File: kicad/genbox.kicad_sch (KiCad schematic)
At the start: 19 parts, among them SW15 SW_SPST, SW16 SW_SPST, SW17 SW_SPST, SW18 SW_SPST

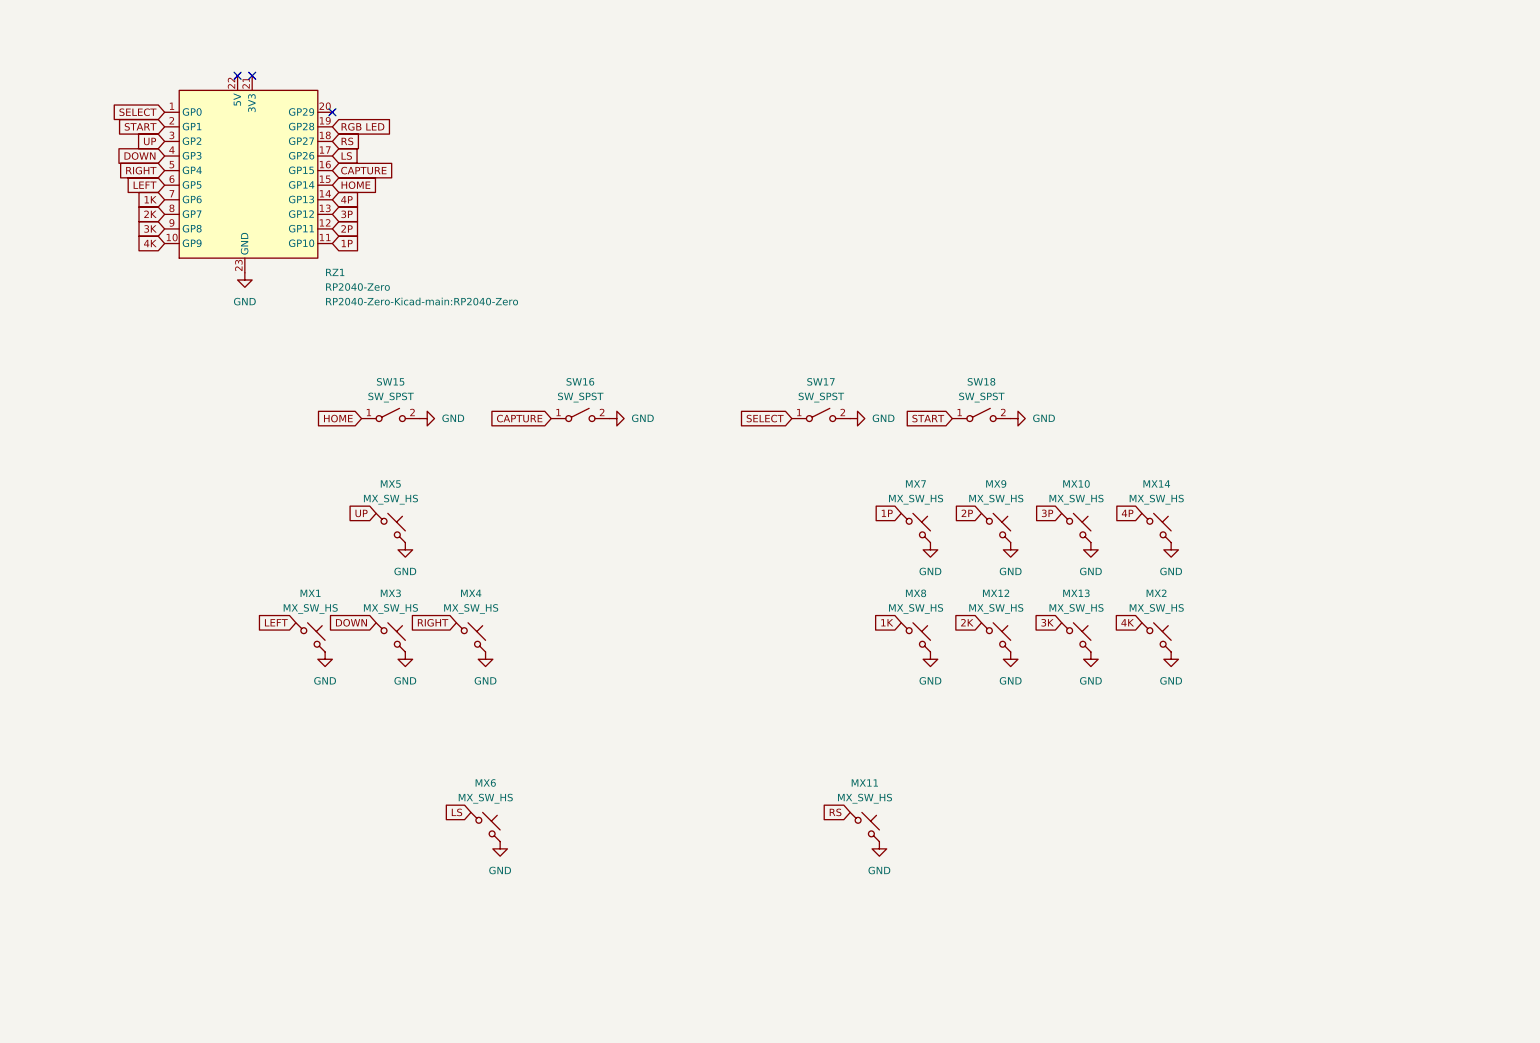
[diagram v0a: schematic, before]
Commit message: fixed gitignore
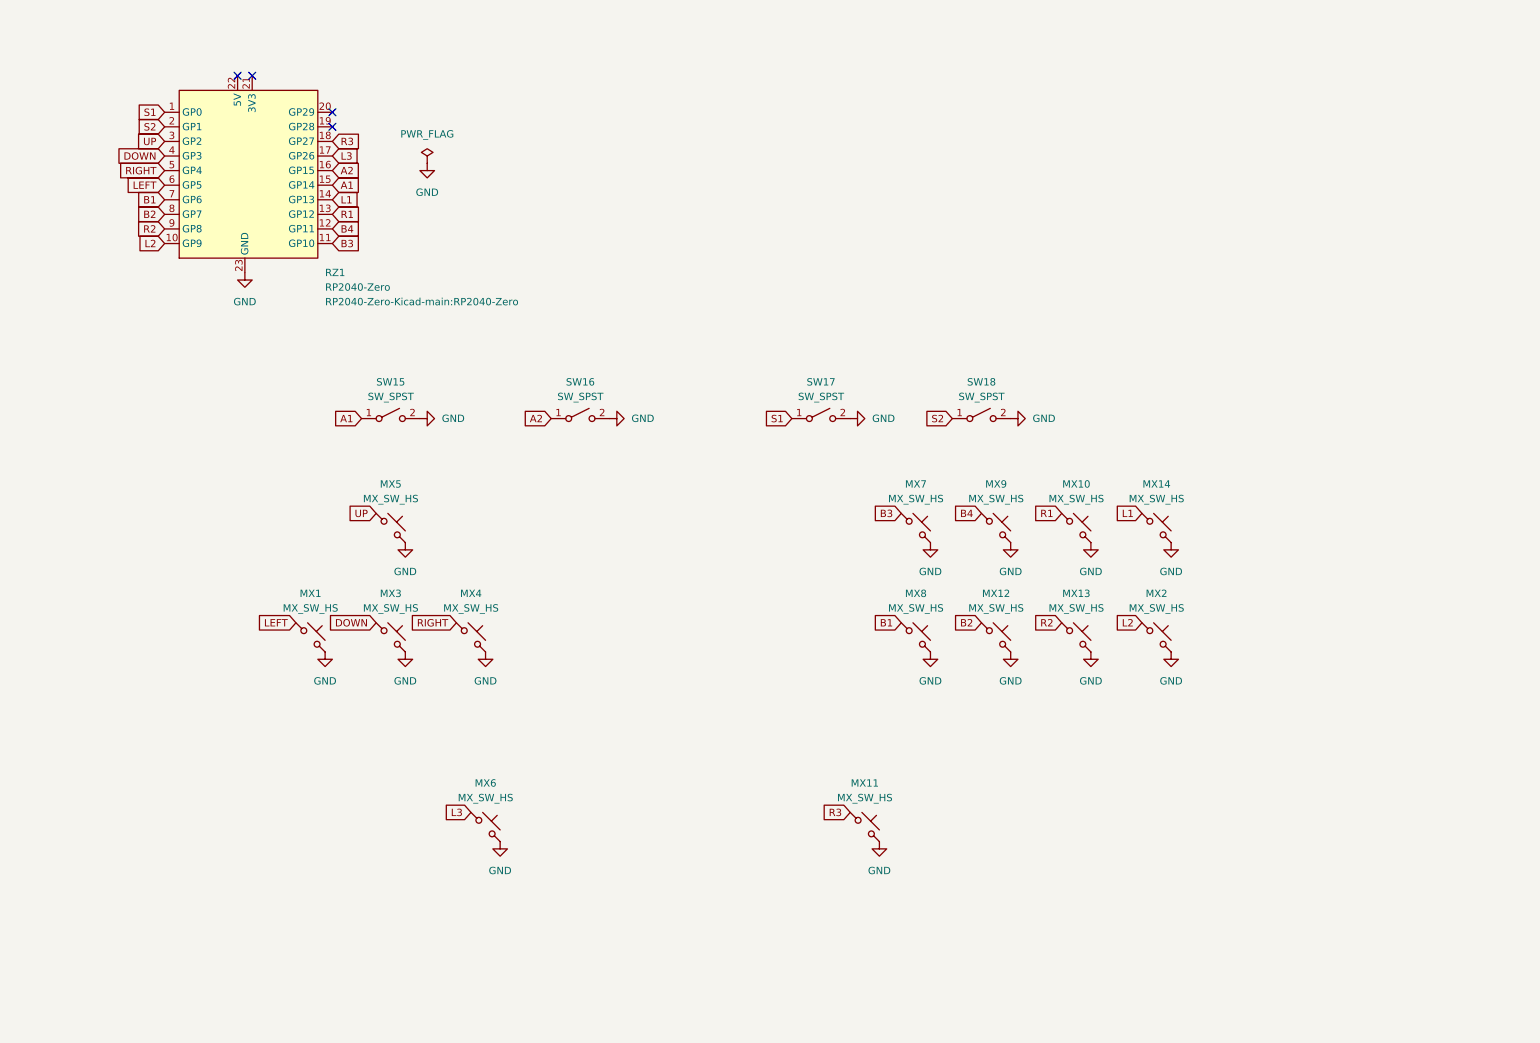
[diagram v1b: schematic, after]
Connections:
- net 1K renamed B1
- net 1P renamed B3
- net 2K renamed B2
- net 2P renamed B4
- net 3K renamed R2
- net 3P renamed R1
- net 4K renamed L2
- net 4P renamed L1
- net CAPTURE renamed A2
- net HOME renamed A1
- net LS renamed L3
- net RGB LED: no longer names the net of RZ1.19 (GP28)
- net RS renamed R3
- net SELECT renamed S1
- net START renamed S2
- no-connect marks 3 -> 4

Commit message: rework p1
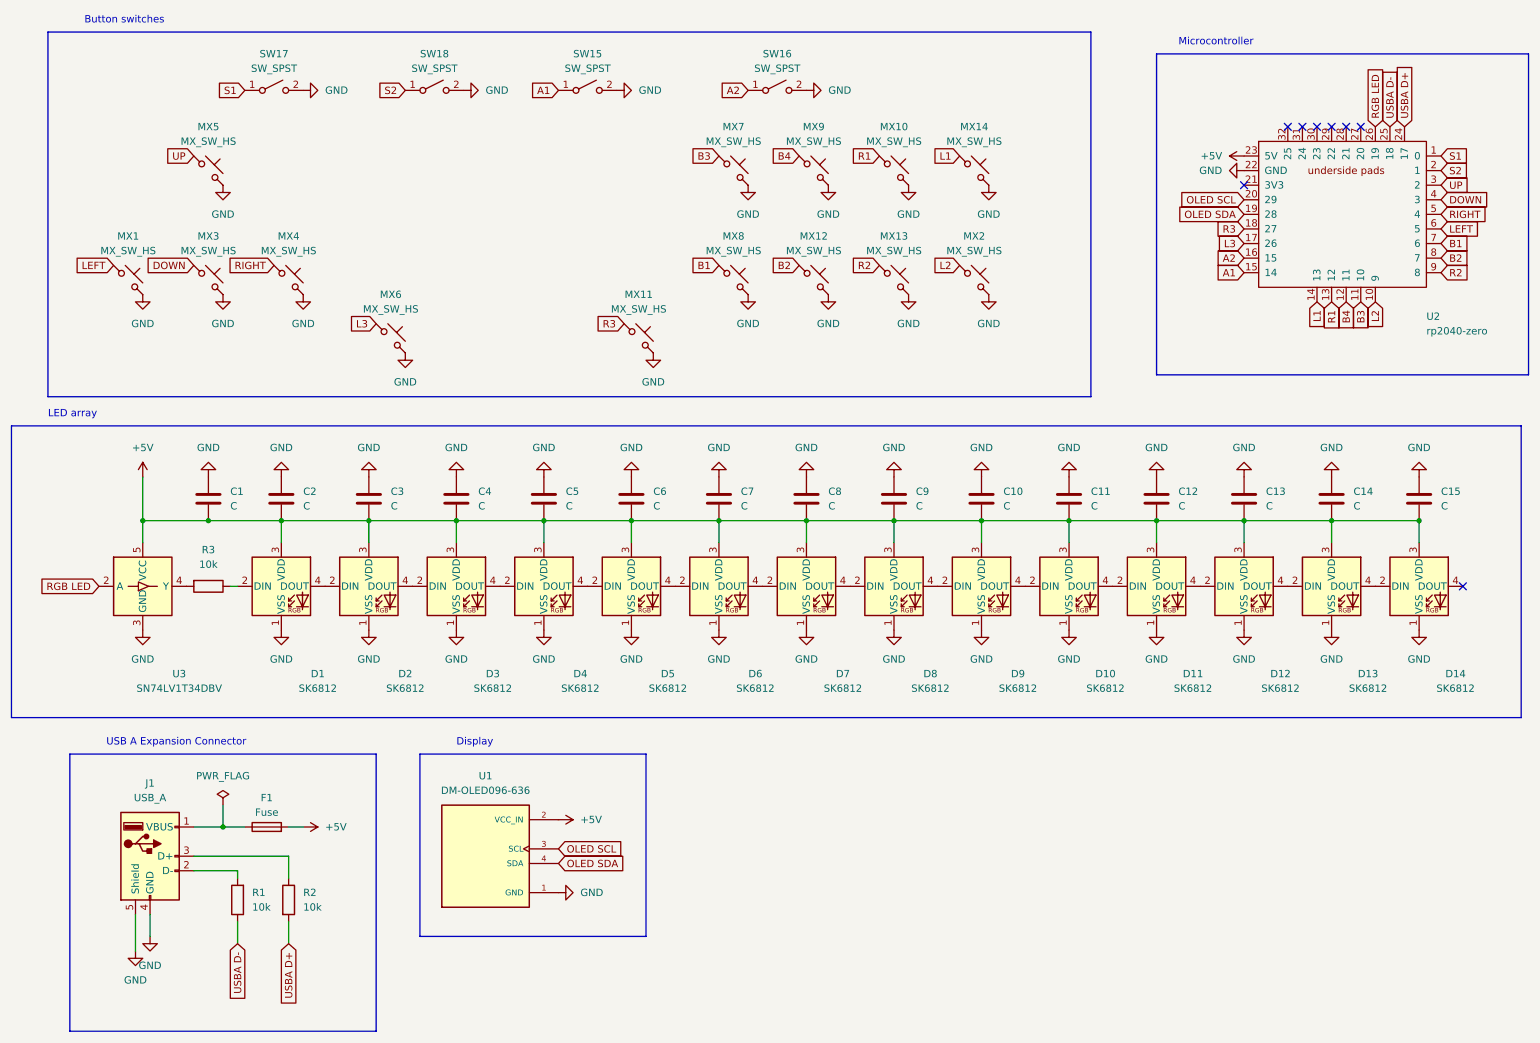
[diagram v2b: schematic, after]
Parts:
- removed RZ1: RP2040-Zero, RP2040-Zero-Kicad-main:RP2040-Zero, symbol rp2040-zero:RP2040-Zero
- added C1, C10, C11, C12, C13, C14, C15, C2, C3, C4, C5, C6, C7, C8, C9: C, Capacitor_SMD:C_0805_2012Metric_Pad1.18x1.45mm_HandSolder, symbol Device:C
- added D1, D10, D11, D12, D13, D14, D2, D3, D4, D5, D6, D7, D8, D9: SK6812, haku:SK6812-MINI-E_MX, symbol LED:SK6812
- added F1: Fuse, Fuse:Fuse_0805_2012Metric_Pad1.15x1.40mm_HandSolder, symbol Device:Fuse
- added J1: USB_A, Connector_USB:USB_A_Receptacle_GCT_USB1046, symbol Connector:USB_A
- added R1, R2, R3: 10k, Resistor_SMD:R_0603_1608Metric_Pad0.98x0.95mm_HandSolder, symbol Device:R
- added U1: DM-OLED096-636, DM-OLED096-636:MODULE_DM-OLED096-636, symbol OLED096:DM-OLED096-636
- added U2: rp2040-zero, mcu:rp2040-zero-smd-pads, symbol mcu:rp2040-zero-pads
- added U3: SN74LV1T34DBV, Package_TO_SOT_SMD:SOT-23-5, symbol Logic_LevelTranslator:SN74LV1T34DBV
- MX1, MX10, MX11, MX12, MX13, MX14, MX2, MX3, MX4, MX5, MX6, MX7, MX8, MX9: LCSC Part # (none) -> C5184526
- SW15, SW16, SW17, SW18: footprint Button_Switch_THT:SW_PUSH_6mm_H7.3mm -> haku:SW_PUSH-12mm_centered; LCSC Part # (none) -> C455212
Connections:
- net A1: now also U2.15 (14)
- net A2: now also U2.16 (15)
- net B1: now also U2.7 (6)
- net B2: now also U2.8 (7)
- net B3: now also U2.11 (10)
- net B4: now also U2.12 (11)
- net DOWN: now also U2.4 (3)
- net GND: now also C1.1, C10.1, C11.1, C12.1, C13.1, C14.1, C15.1, C2.1, C3.1, C4.1, C5.1, C6.1, C7.1, C8.1, C9.1, D1.1 (VSS), D10.1 (VSS), D11.1 (VSS), D12.1 (VSS), D13.1 (VSS), D14.1 (VSS), D2.1 (VSS), D3.1 (VSS), D4.1 (VSS), D5.1 (VSS), D6.1 (VSS), D7.1 (VSS), D8.1 (VSS), D9.1 (VSS), J1.4 (GND), J1.5 (Shield), U1.1 (GND), U2.22 (GND), U2.33 (GND), U3.3 (GND)
- net L1: now also U2.14 (13)
- net L2: now also U2.10 (9)
- net L3: now also U2.17 (26)
- net LEFT: now also U2.6 (5)
- net R1: now also U2.13 (12)
- net R2: now also U2.9 (8)
- net R3: now also U2.18 (27)
- net RIGHT: now also U2.5 (4)
- net S1: now also U2.1 (0)
- net S2: now also U2.2 (1)
- net UP: now also U2.3 (2)
- new net: D13.4 (DOUT), D14.2 (DIN)
- new net: D3.4 (DOUT), D4.2 (DIN)
- new net: D4.4 (DOUT), D5.2 (DIN)
- new net: D1.2 (DIN), R3.1
- new net: D1.4 (DOUT), D2.2 (DIN)
- new net: D6.4 (DOUT), D7.2 (DIN)
- new net: D7.4 (DOUT), D8.2 (DIN)
- new net: D8.4 (DOUT), D9.2 (DIN)
- new net: D10.2 (DIN), D9.4 (DOUT)
- new net: D5.4 (DOUT), D6.2 (DIN)
- new net: F1.1, J1.1 (VBUS)
- new net: J1.2 (D-), R1.2
- new net: J1.3 (D+), R2.1
- new net: D10.4 (DOUT), D11.2 (DIN)
- new net: R3.2, U3.4 (Y)
- new net: D11.4 (DOUT), D12.2 (DIN)
- new net: D2.4 (DOUT), D3.2 (DIN)
- new net: D12.4 (DOUT), D13.2 (DIN)
- new net +5V: C1.2, C10.2, C11.2, C12.2, C13.2, C14.2, C15.2, C2.2, C3.2, C4.2, C5.2, C6.2, C7.2, C8.2, C9.2, D1.3 (VDD), D10.3 (VDD), D11.3 (VDD), D12.3 (VDD), D13.3 (VDD), D14.3 (VDD), D2.3 (VDD), D3.3 (VDD), D4.3 (VDD), D5.3 (VDD), D6.3 (VDD), D7.3 (VDD), D8.3 (VDD), D9.3 (VDD), F1.2, U1.2 (VCC_IN), U2.23 (5V), U3.5 (VCC)
- new net OLED SCL: U1.3 (SCL), U2.20 (29)
- new net OLED SDA: U1.4 (SDA), U2.19 (28)
- new net RGB LED: U2.26 (19), U3.2 (A)
- new net USBA D+: R2.2, U2.24 (17)
- new net USBA D-: R1.1, U2.25 (18)
- no-connect marks 4 -> 8
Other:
- note added: "Button switches"
- note added: "Display"
- note added: "LED array"
- note added: "Microcontroller"
- note added: "USB A Expansion Connector"
- moved on the sheet: MX1, MX10, MX11, MX12, MX13, MX14, MX2, MX3, MX4, MX5, MX6, MX7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

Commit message: converted to freecad link branch
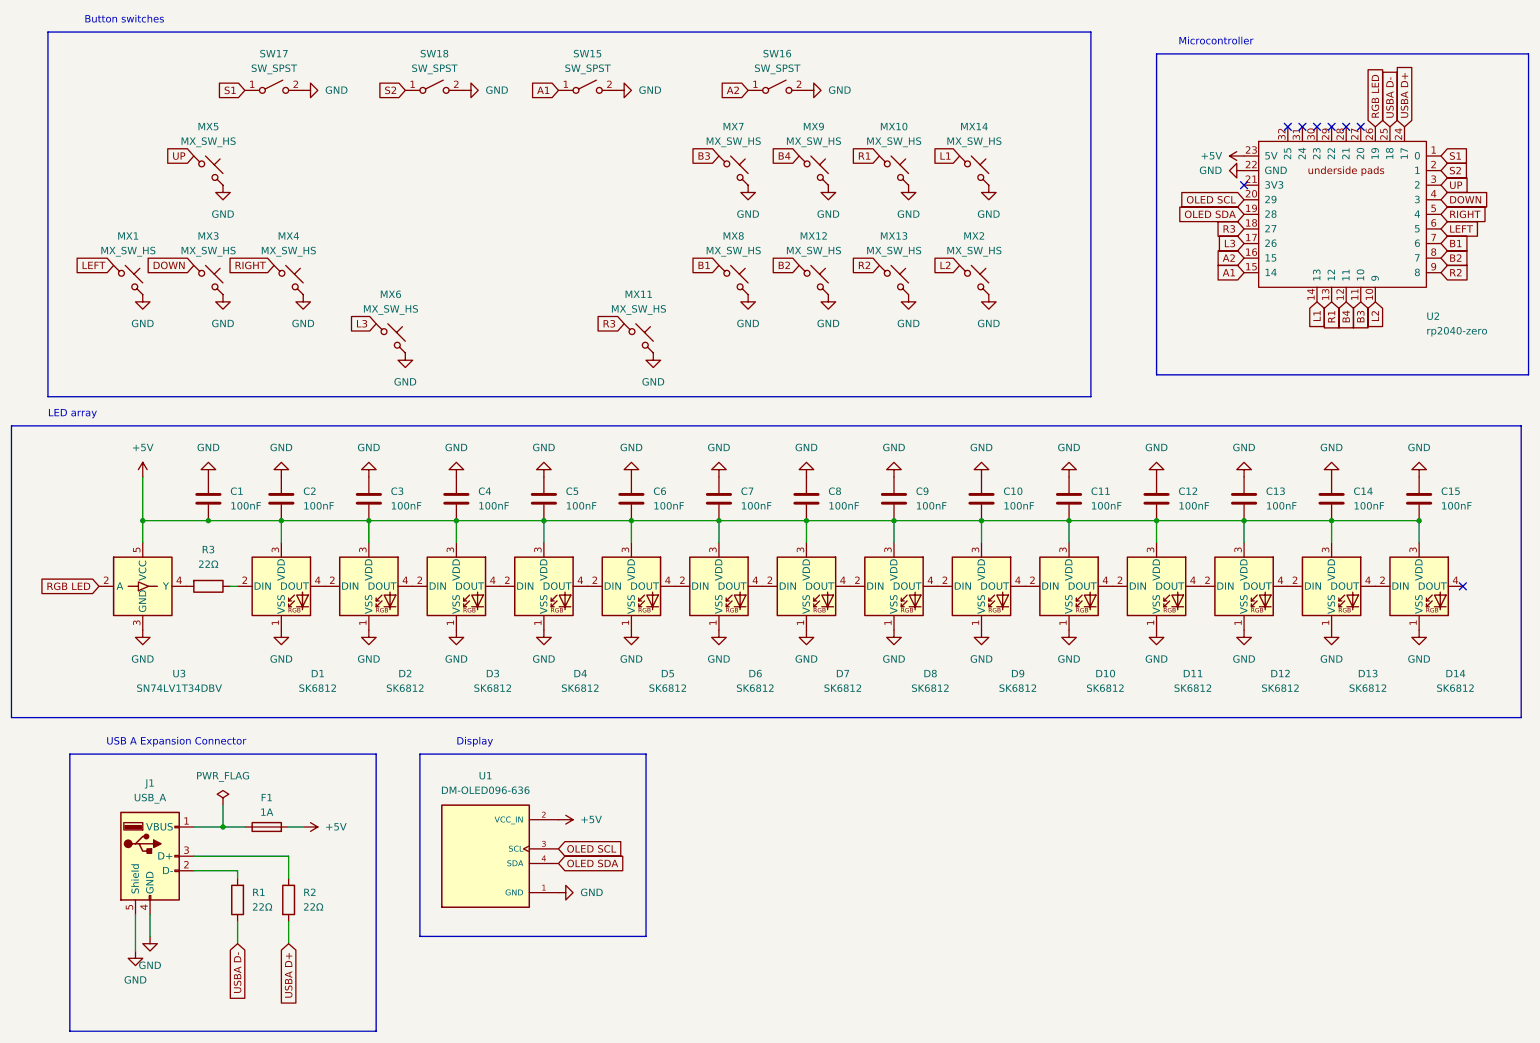
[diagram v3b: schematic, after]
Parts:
- C1, C10, C11, C12, C13, C14, C15, C2, C3, C4, C5, C6, C7, C8, C9: value C -> 100nF
- F1: value Fuse -> 1A
- R1, R2, R3: value 10k -> 22Ω
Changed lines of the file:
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@@
       (effects (font (size 1.27 1.27)) (justify left))
     )
-    (property "Value" "C" (at 187.96 101.6 0)
+    (property "Value" "100nF" (at 187.96 101.6 0)
       (effects (font (size 1.27 1.27)) (justify left))
     )
@@
       (effects (font (size 1.27 1.27)) (justify left))
     )
-    (property "Value" "C" (at 248.92 101.6 0)
+    (property "Value" "100nF" (at 248.92 101.6 0)
       (effects (font (size 1.27 1.27)) (justify left))
     )
@@
       (effects (font (size 1.27 1.27)) (justify left))
     )
-    (property "Value" "C" (at 96.52 101.6 0)
+    (property "Value" "100nF" (at 96.52 101.6 0)
       (effects (font (size 1.27 1.27)) (justify left))
     )
@@
       (effects (font (size 1.27 1.27)) (justify left))
     )
-    (property "Value" "C" (at 264.16 101.6 0)
+    (property "Value" "100nF" (at 264.16 101.6 0)
       (effects (font (size 1.27 1.27)) (justify left))
     )
@@
       (effects (font (size 1.27 1.27)) (justify left))
     )
-    (property "Value" "C" (at 218.44 101.6 0)
+    (property "Value" "100nF" (at 218.44 101.6 0)
       (effects (font (size 1.27 1.27)) (justify left))
     )
@@
       (effects (font (size 1.27 1.27)) (justify left))
     )
-    (property "Value" "C" (at 157.48 101.6 0)
+    (property "Value" "100nF" (at 157.48 101.6 0)
       (effects (font (size 1.27 1.27)) (justify left))
     )
@@
       (effects (font (size 1.27 1.27)) (justify left))
     )
-    (property "Value" "C" (at 203.2 101.6 0)
+    (property "Value" "100nF" (at 203.2 101.6 0)
       (effects (font (size 1.27 1.27)) (justify left))
     )
@@
       (effects (font (size 1.27 1.27)) (justify left))
     )
-    (property "Value" "C" (at 81.28 101.6 0)
+    (property "Value" "100nF" (at 81.28 101.6 0)
       (effects (font (size 1.27 1.27)) (justify left))
     )
@@
       (effects (font (size 1.27 1.27)) (justify left))
     )
-    (property "Value" "C" (at 111.76 101.6 0)
+    (property "Value" "100nF" (at 111.76 101.6 0)
       (effects (font (size 1.27 1.27)) (justify left))
     )
@@
       (effects (font (size 1.27 1.27)) (justify left))
     )
-    (property "Value" "C" (at 66.04 101.6 0)
+    (property "Value" "100nF" (at 66.04 101.6 0)
       (effects (font (size 1.27 1.27)) (justify left))
     )
@@
       (effects (font (size 1.27 1.27)) (justify left))
     )
-    (property "Value" "C" (at 233.68 101.6 0)
+    (property "Value" "100nF" (at 233.68 101.6 0)
       (effects (font (size 1.27 1.27)) (justify left))
     )
@@
       (effects (font (size 1.27 1.27)) (justify left))
     )
-    (property "Value" "10k" (at 66.04 171.45 0)
+    (property "Value" "22Ω" (at 66.04 171.45 0)
       (effects (font (size 1.27 1.27)) (justify left))
     )
@@
       (effects (font (size 1.27 1.27)) (justify left))
     )
-    (property "Value" "C" (at 53.34 101.6 0)
+    (property "Value" "100nF" (at 53.34 101.6 0)
       (effects (font (size 1.27 1.27)) (justify left))
     )
@@
       (effects (font (size 1.27 1.27)))
     )
-    (property "Value" "10k" (at 49.53 111.76 90)
+    (property "Value" "22Ω" (at 49.53 111.76 90)
       (effects (font (size 1.27 1.27)))
     )
@@
       (effects (font (size 1.27 1.27)) (justify left))
     )
-    (property "Value" "C" (at 127 101.6 0)
+    (property "Value" "100nF" (at 127 101.6 0)
       (effects (font (size 1.27 1.27)) (justify left))
     )
@@
       (effects (font (size 1.27 1.27)) (justify left))
     )
-    (property "Value" "C" (at 172.72 101.6 0)
+    (property "Value" "100nF" (at 172.72 101.6 0)
       (effects (font (size 1.27 1.27)) (justify left))
     )
@@
       (effects (font (size 1.27 1.27)) (justify left))
     )
-    (property "Value" "C" (at 142.24 101.6 0)
+    (property "Value" "100nF" (at 142.24 101.6 0)
       (effects (font (size 1.27 1.27)) (justify left))
     )
@@
       (effects (font (size 1.27 1.27)) (justify right))
     )
-    (property "Value" "10k" (at 57.15 171.45 0)
+    (property "Value" "22Ω" (at 57.15 171.45 0)
       (effects (font (size 1.27 1.27)) (justify right))
     )
@@
       (effects (font (size 1.27 1.27)))
     )
-    (property "Value" "Fuse" (at 59.69 154.94 90)
-      (effects (font (size 1.27 1.27)))
-    )
+    (property "Value" "1A" (at 59.69 154.94 90)
+      (effects (font (size 1.27 1.27)))
+    )

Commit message: pcb rework complete
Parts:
- SW15, SW16, SW17, SW18: symbol Switch:SW_SPST -> Switch:SW_Push_Dual_x2
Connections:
- net A1: now also U2.19 (28); no longer U2.15 (14)
- net A2: now also U2.20 (29); no longer U2.16 (15)
- net B1: now also U2.11 (10); no longer U2.7 (6)
- net B2: now also U2.13 (12); no longer U2.8 (7)
- net B3: now also U2.12 (11); no longer U2.11 (10)
- net B4: now also U2.14 (13); no longer U2.12 (11)
- net DOWN: now also U2.6 (5); no longer U2.4 (3)
- net L1: now also U2.25 (18); no longer U2.14 (13)
- net L2: now also U2.24 (17); no longer U2.10 (9)
- net L3: now also U2.9 (8); no longer U2.17 (26)
- net LEFT: now also U2.7 (6); no longer U2.6 (5)
- net OLED SCL: now also U2.3 (2); no longer U2.20 (29)
- net OLED SDA: now also U2.4 (3); no longer U2.19 (28)
- net R1: now also U2.16 (15); no longer U2.13 (12)
- net R2: now also U2.15 (14); no longer U2.9 (8)
- net R3: now also U2.10 (9); no longer U2.18 (27)
- net RIGHT: now also U2.8 (7); no longer U2.5 (4)
- net S1: now also U2.17 (26); no longer U2.1 (0)
- net S2: now also U2.18 (27); no longer U2.2 (1)
- net UP: now also U2.5 (4); no longer U2.3 (2)
- net USBA D+: now also U2.1 (0); no longer U2.24 (17)
- net USBA D-: now also U2.2 (1); no longer U2.25 (18)
